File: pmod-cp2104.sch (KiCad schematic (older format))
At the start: 35 parts, among them P1 PMOD-CONN_6X2

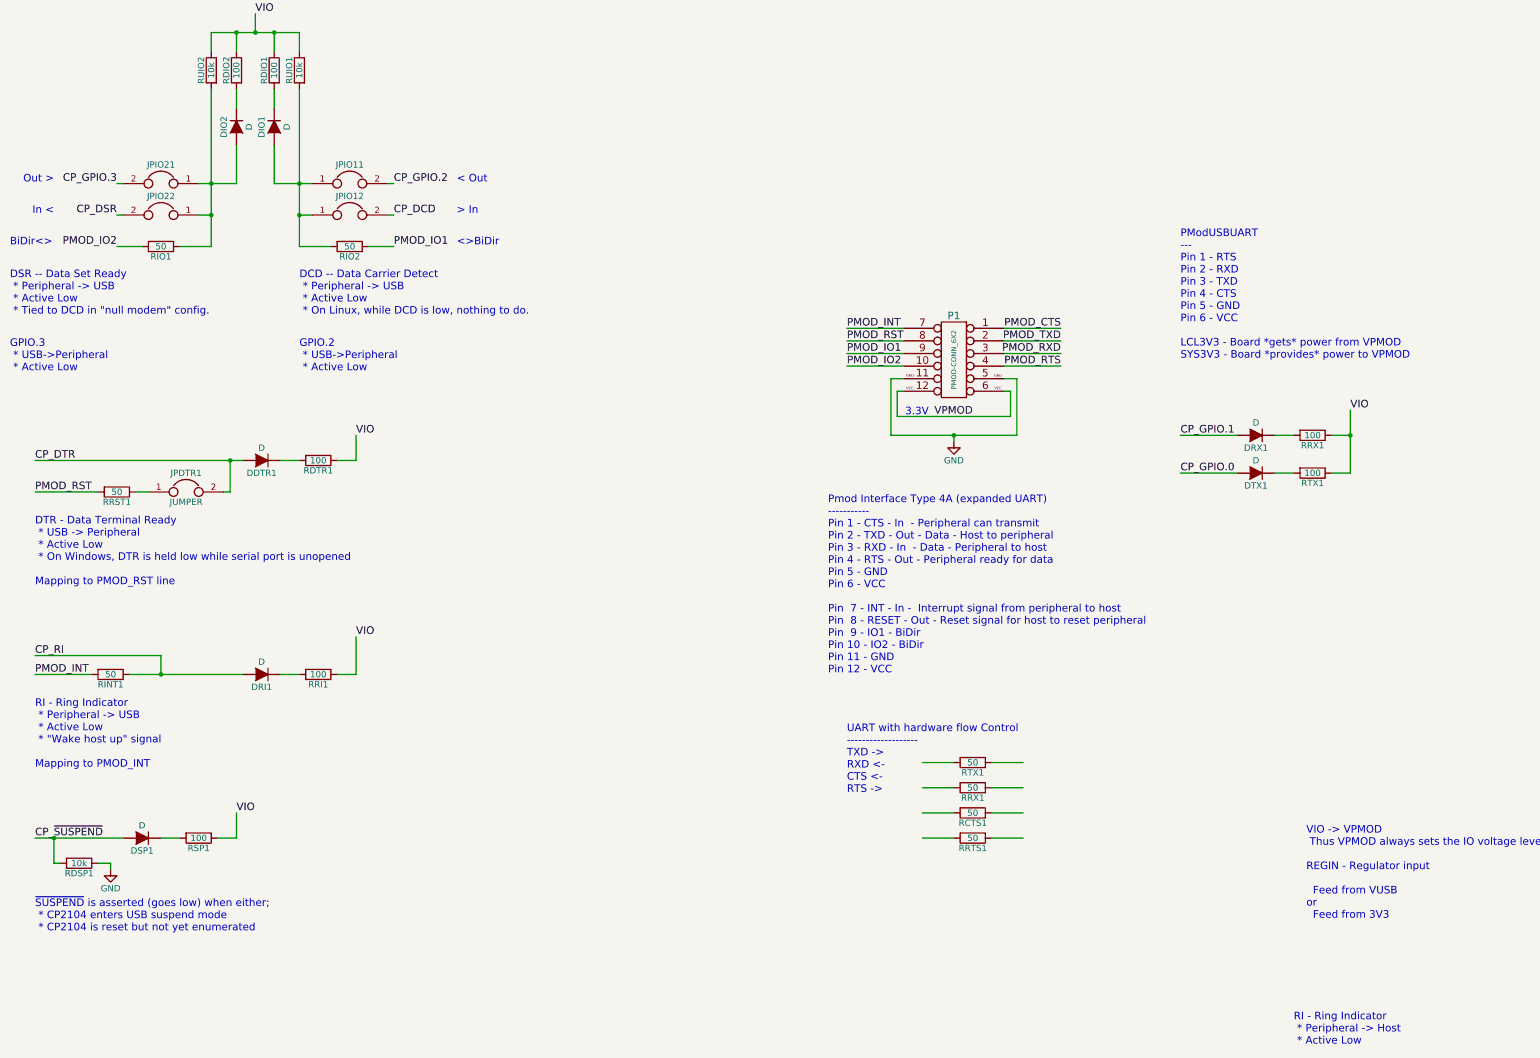
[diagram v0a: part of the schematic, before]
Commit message: Move the protection resistors to around the pmod header.
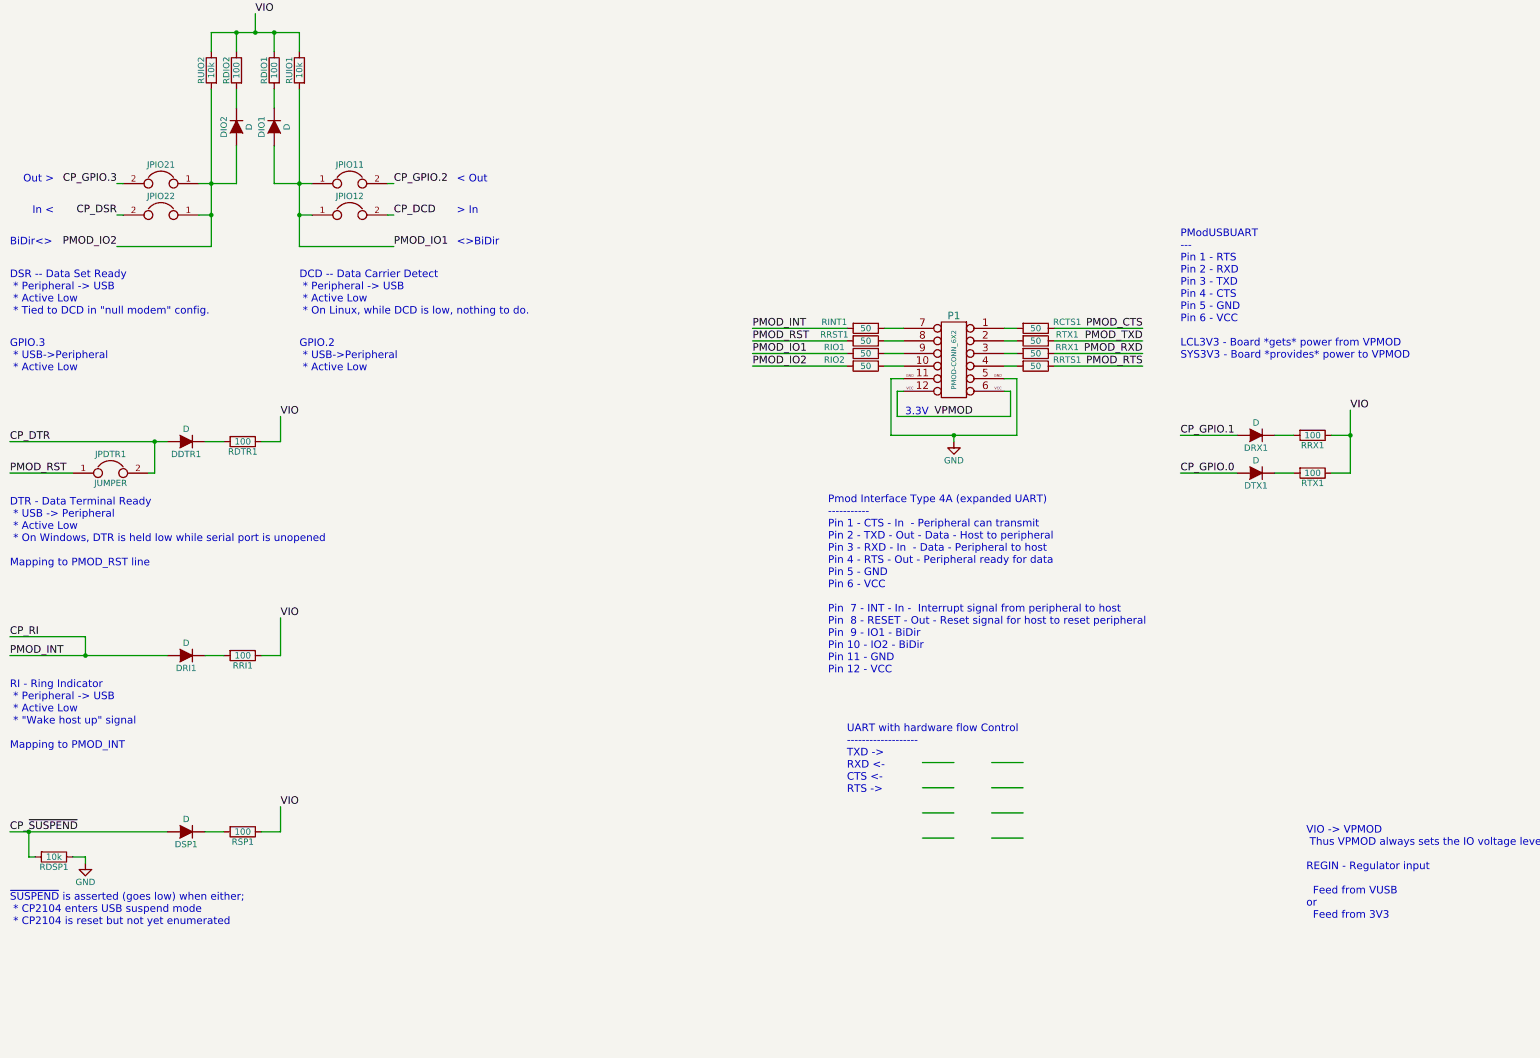
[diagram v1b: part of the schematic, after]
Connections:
- wire segments 113 -> 117
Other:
- note removed: "RI - Ring Indicator\n * Peripheral -> Host\n * Active Low"
- moved on the sheet: DDTR1, DRI1, DSP1, JPDTR1, RCTS1, RDSP1, RDTR1, RINT1, RIO1, RIO2, RRI1, RRST1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

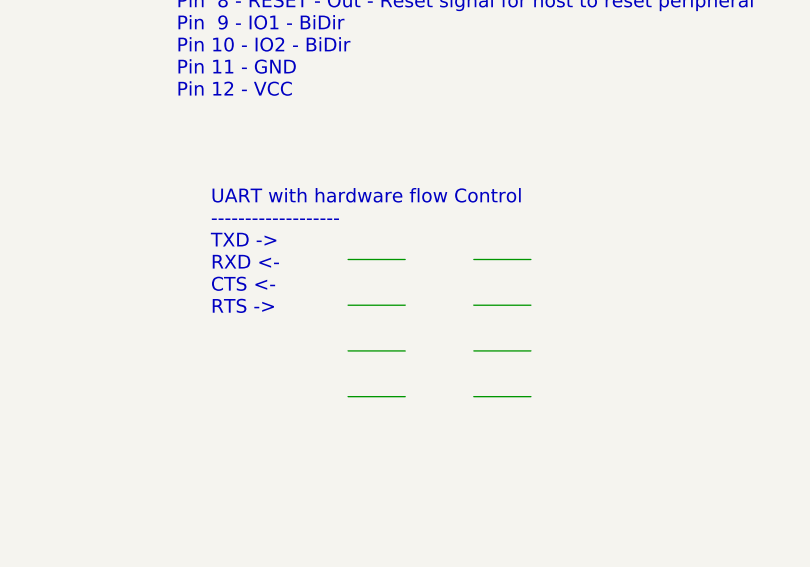
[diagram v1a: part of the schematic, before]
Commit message: Remove some unused wires.
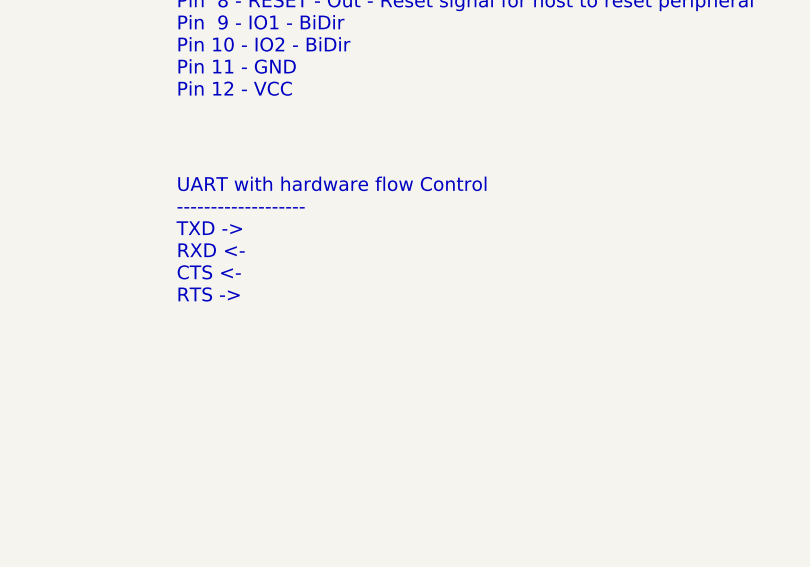
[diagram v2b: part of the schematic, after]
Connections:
- wire segments 117 -> 109
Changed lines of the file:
@@
 	-1   0    0    -1
 $EndComp
-Text Notes 1350 5150 0    60   ~ 0
+Text Notes 1200 5100 0    60   ~ 0
 UART with hardware flow Control\n-------------------\nTXD ->\nRXD <-\nCTS <-\nRTS ->\n
 $Comp
@@
 	0    1    1    0
 $EndComp
-Wire Wire Line
-	1950 4900 2200 4900
-Wire Wire Line
-	1950 5100 2200 5100
-Wire Wire Line
-	1950 5300 2200 5300
-Wire Wire Line
-	1950 5500 2200 5500
-Wire Wire Line
-	2500 4900 2750 4900
-Wire Wire Line
-	2500 5100 2750 5100
-Wire Wire Line
-	2500 5300 2750 5300
-Wire Wire Line
-	2500 5500 2750 5500
 $Comp
 L D DSP1

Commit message: Rearranging things a little.
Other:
- note added: "Transmit and Receive indicator LEDs"
- moved on the sheet: DRX1, DTX1, P1, RCTS1, RINT1, RIO1, RIO2, RRST1, RRTS1, RRX1, RTX1

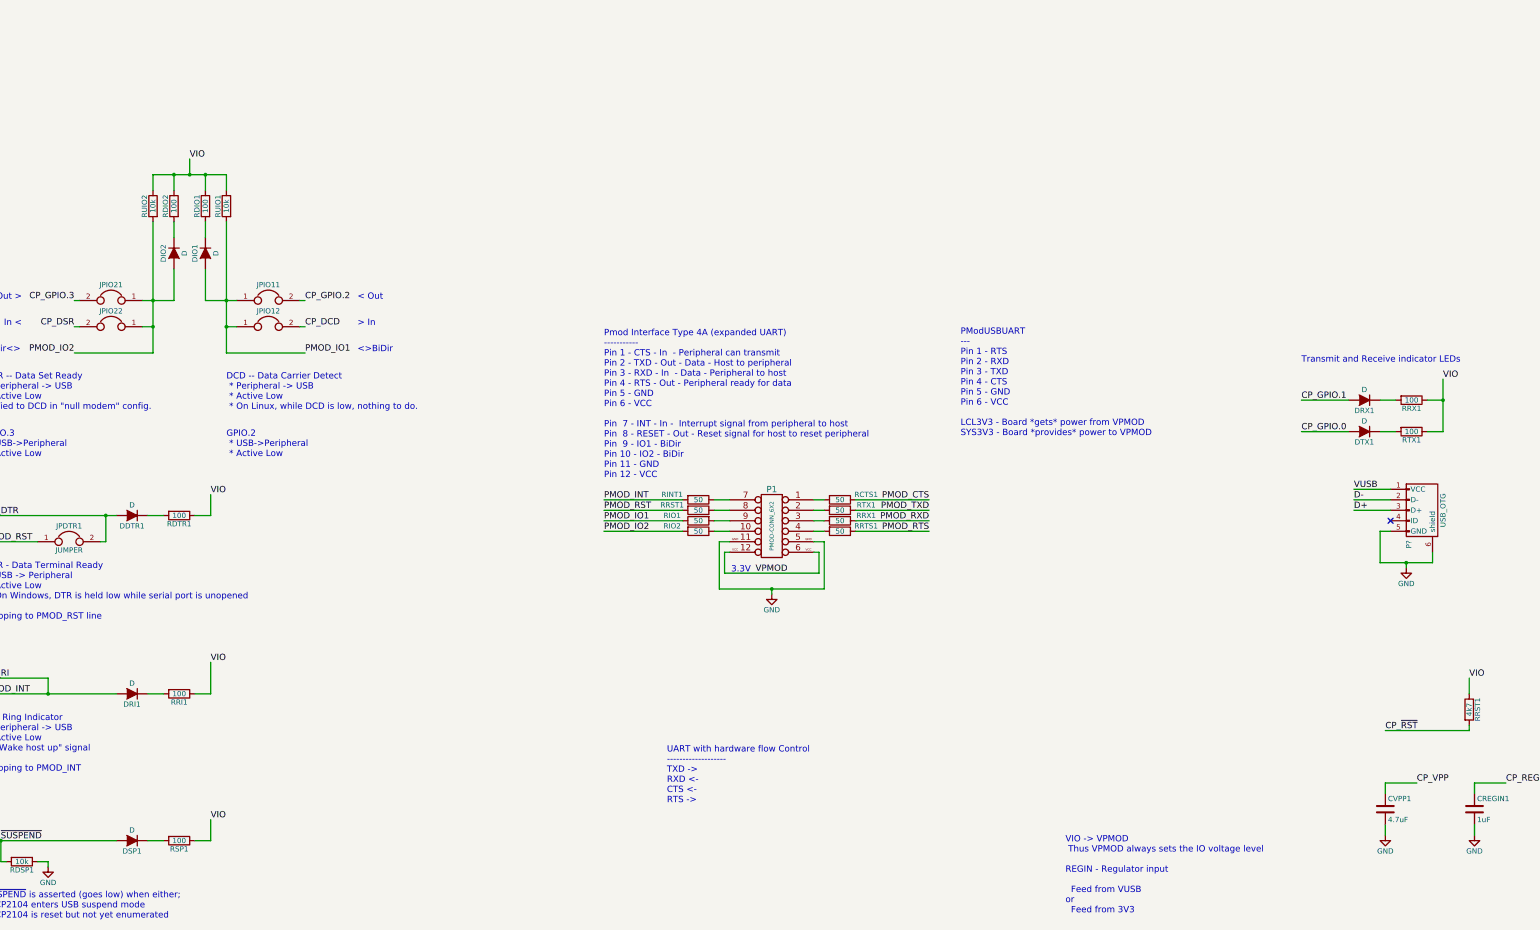
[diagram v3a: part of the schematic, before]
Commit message: Make the LEDs be between VIO and VDD.
 * High - LED is off
 * Low - LED is on
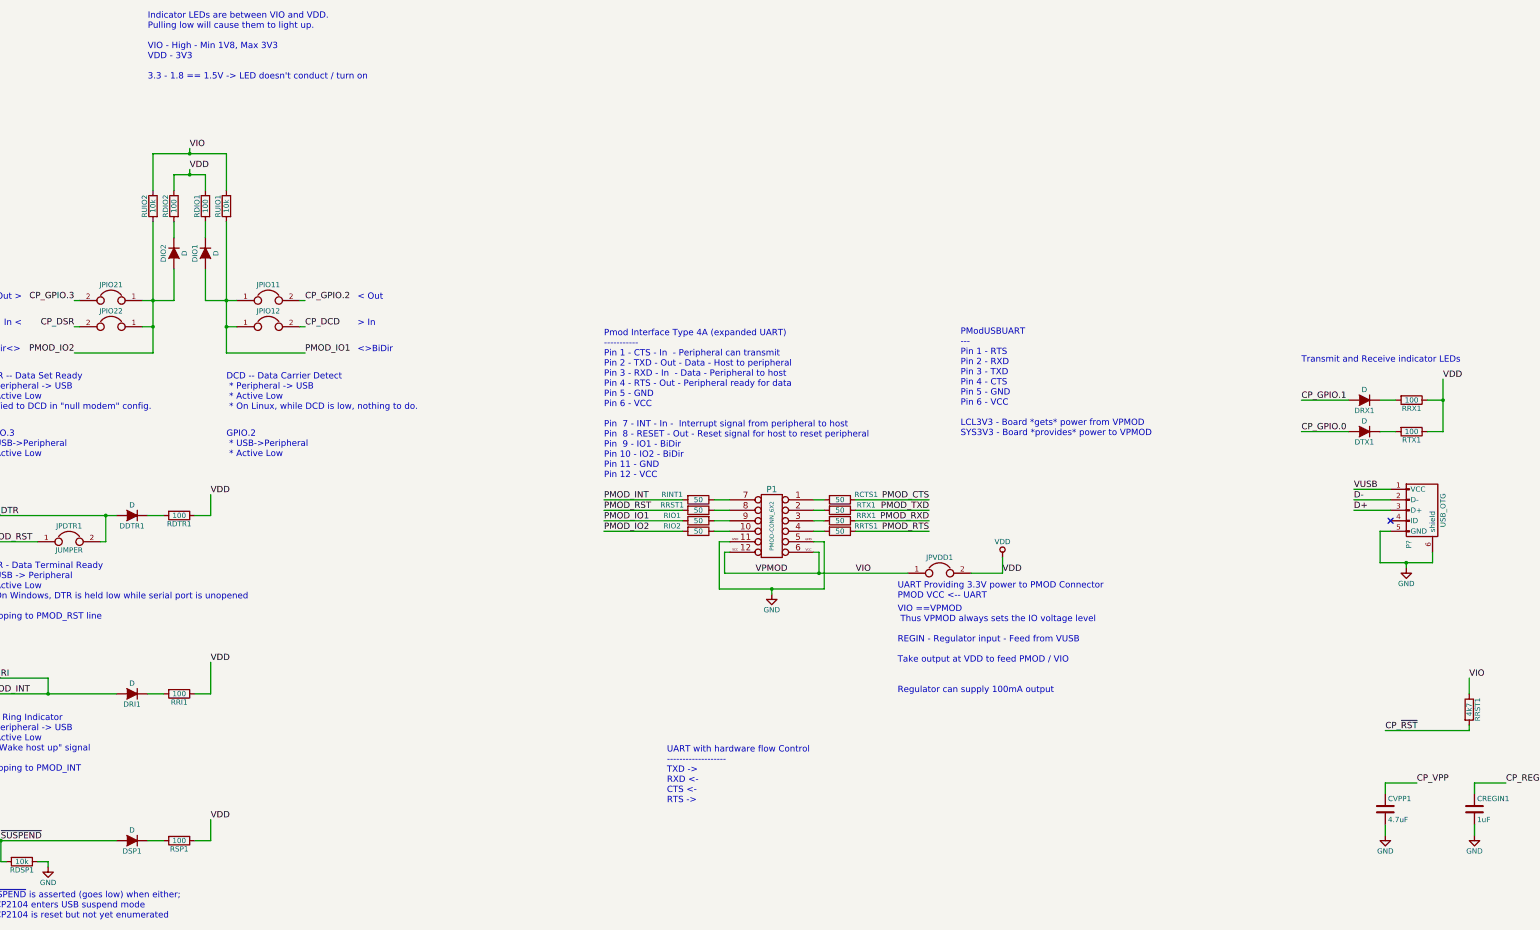
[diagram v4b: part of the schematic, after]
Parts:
- added JPVDD1: JUMPER, symbol JUMPER
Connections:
- net VPMOD is gone; now on net VIO: P1.12 (P12), P1.6 (P6)
- net VIO: now also JPVDD1.1; no longer RDIO1.1, RDIO2.1, RDTR1.1, RRI1.1, RRX1.1, RSP1.1, RTX1.1
- new net VDD: JPVDD1.2, RDIO1.1, RDIO2.1, RDTR1.1, RRI1.1, RRX1.1, RSP1.1, RTX1.1
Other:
- note added: "Indicator LEDs are between VIO and VDD. \nPulling low will cause them to light up.\n\nVIO - High - Min 1V8, Max 3V3\nVDD - 3V3\n\n3.3 - 1.8 == 1.5V -> LED doesn't conduct / turn on\n"
- note added: "UART Providing 3.3V power to PMOD Connector\nPMOD VCC <-- UART"
- note added: "VIO ==VPMOD\n Thus VPMOD always sets the IO voltage level\n\nREGIN - Regulator input - Feed from VUSB\n\nTake output at VDD to feed PMOD / VIO\n\n\nRegulator can supply 100mA output"
- note removed: "3.3V"
- note removed: "VIO -> VPMOD\n Thus VPMOD always sets the IO voltage level\n\nREGIN - Regulator input \n\n Feed from VUSB\nor\n Feed from 3V3"
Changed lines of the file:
@@
 	1750 2900 2650 2900
 Wire Wire Line
+	2650 2900 3500 2900
+Wire Wire Line
 	2650 2900 2650 2700
 Wire Wire Line
@@
 	2600 2600 2700 2600
 Wire Wire Line
-	2700 2600 2700 3050
-Wire Wire Line
-	2700 3050 2200 3050
-Wire Wire Line
-	2200 3050 1700 3050
+	2700 3050 2700 2600
+Wire Wire Line
+	1700 3050 2200 3050
+Wire Wire Line
+	2200 3050 2700 3050
 Wire Wire Line
 	1700 3050 1700 2600
 Wire Wire Line
 	1700 2600 1800 2600
-Text Notes 2000 2900 2    60   ~ 0
-3.3V
 $Comp
 L GND #PWR?
@@
 Text Notes 4000 1600 0    60   ~ 0
 PModUSBUART\n---\nPin 1 - RTS\nPin 2 - RXD\nPin 3 - TXD\nPin 4 - CTS\nPin 5 - GND\nPin 6 - VCC\n\nLCL3V3 - Board *gets* power from VPMOD\nSYS3V3 - Board *provides* power to VPMOD
-Text Notes 5000 6150 0    60   ~ 0
-VIO -> VPMOD\n Thus VPMOD always sets the IO voltage level\n\nREGIN - Regulator input \n\n  Feed from VUSB\nor\n  Feed from 3V3
+Text Notes 3400 4050 0    60   ~ 0
+VIO ==VPMOD\n Thus VPMOD always sets the IO voltage level\n\nREGIN - Regulator input - Feed from VUSB\n\nTake output at VDD to feed PMOD / VIO\n\n\nRegulator can supply 100mA output
 Text Label 8050 4400 0    60   ~ 0
 CP_~RST
@@
 	8000 1550 8150 1550
 Text Label 8600 1050 0    60   ~ 0
-VIO
+VDD
 Wire Wire Line
 	7700 1250 7250 1250
@@
 	-3600 2350 -3750 2350
 Text Label -3150 2150 0    60   ~ 0
-VIO
+VDD
 Wire Wire Line
 	-5300 2350 -4150 2350
@@
 CP_RI
 Text Label -3150 3750 0    60   ~ 0
-VIO
+VDD
 $Comp
 L R RINT1
@@
 Wire Wire Line
 	-3500 -300 -3500 -450
-Text Label -3350 -1050 0    60   ~ 0
+Text Label -3350 -1150 0    60   ~ 0
 VIO
 Wire Wire Line
@@
 CP_GPIO.2
 Wire Wire Line
-	-3700 -900 -3500 -900
-Wire Wire Line
-	-3500 -900 -3350 -900
-Wire Wire Line
-	-3350 -900 -3200 -900
-Wire Wire Line
-	-3200 -900 -3000 -900
-Wire Wire Line
-	-3350 -900 -3350 -1050
+	-3350 -900 -3350 -950
 Connection ~ -3350 -900
 Wire Wire Line
@@
 $EndComp
 Wire Wire Line
-	-3000 -900 -3000 -750
-Connection ~ -3200 -900
+	-3000 -1100 -3000 -750
 Text Notes -1750 300  0    60   ~ 0
 < Out
@@
 BiDir<>
 Wire Wire Line
-	-3700 800  -3700 550
-Wire Wire Line
-	-3700 550  -3700 300
-Wire Wire Line
-	-3700 300  -3700 -450
+	-3700 -450 -3700 300
+Wire Wire Line
+	-3700 300  -3700 550
+Wire Wire Line
+	-3700 550  -3700 800
 $Comp
 L R RUIO2
@@
 $EndComp
 Wire Wire Line
-	-3700 -900 -3700 -750
-Connection ~ -3500 -900
+	-3700 -1100 -3700 -750
 Connection ~ -3700 550
 $Comp
@@
 	-3600 5450 -3750 5450
 Text Label -3150 5250 0    60   ~ 0
-VIO
+VDD
 Wire Wire Line
 	-5300 5450 -5150 5450
@@
 $EndComp
 Wire Wire Line
-	-4450 800  -3700 800
+	-3700 800  -4450 800
 $Comp
 L JUMPER JPIO21
@@
 Text Notes 7250 900  0    60   ~ 0
 Transmit and Receive indicator LEDs
+Connection ~ 2650 2900
+Text Label 3000 2900 0    60   ~ 0
+VIO
+$Comp
+L JUMPER JPVDD1
+U 1 1 57F5C981
+P 3800 2900
+F 0 "JPVDD1" H 3800 3050 50  0000 C CNN
+F 1 "JUMPER" H 3800 2820 50  0001 C CNN
+F 2 "" H 3800 2900 50  0000 C CNN
+F 3 "" H 3800 2900 50  0000 C CNN
+	1    3800 2900
+	1    0    0    -1
+$EndComp
+Wire Wire Line
+	4100 2900 4400 2900
+Text Label 4400 2900 0    60   ~ 0
+VDD
+$Comp
+L VDD #PWR?
+U 1 1 57F5D066
+P 4400 2750
+F 0 "#PWR?" H 4400 2600 50  0001 C CNN
+F 1 "VDD" H 4400 2900 50  0000 C CNN
+F 2 "" H 4400 2750 50  0000 C CNN
+F 3 "" H 4400 2750 50  0000 C CNN
+	1    4400 2750
+	1    0    0    -1
+$EndComp
+Wire Wire Line
+	4400 2900 4400 2750
+Text Notes 3400 3150 0    60   ~ 0
+UART Providing 3.3V power to PMOD Connector\nPMOD VCC <-- UART
+Text Label -3350 -950 0    60   ~ 0
+VDD
+Wire Wire Line
+	-3500 -900 -3350 -900
+Wire Wire Line
+	-3350 -900 -3200 -900
+Wire Wire Line
+	-3700 -1100 -3350 -1100
+Wire Wire Line
+	-3350 -1100 -3000 -1100
+Wire Wire Line
+	-3350 -1100 -3350 -1150
+Connection ~ -3350 -1100
+Text Notes -3750 -1800 0    60   ~ 0
+Indicator LEDs are between VIO and VDD. \nPulling low will cause them to light up.\n\nVIO - High - Min 1V8, Max 3V3\nVDD - 3V3\n\n3.3 - 1.8 == 1.5V -> LED doesn't conduct / turn on\n
 $EndSCHEMATC
